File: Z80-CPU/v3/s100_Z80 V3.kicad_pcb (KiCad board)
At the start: 2 copper layers, 254 x 134.6 mm, 164 parts, among them K1 CONN_3, K10 U15 Clock, K11 bA13, K12 bA12, K13 bA19, K14 bA18, K15 bA16, K16 bA17, K17 EN_WAITS, K18 ROM_E-, K2 CONN_3, K3 pSYNCdata, K4 CONN_3, K5 pSYNC, K6 bA15, K7 bA14, K8 WRstrobe, K9 U29B Q, P1 S100_MALE, P2 CONN_4X2, P3 CLK_CPU, P34 CONN_1, P35 CONN_1, P36 CONN_3X2, P4 CONN_2X2, P5 CLK_CPU, P6 MASTER_OSC, P7 CLK_SEL, Q2 ^^NPN-SOT23, Q3 ^^NPN-SOT23, Q4 ^^NPN-SOT23, Q5 ^^NPN-SOT23, Q6 ^^NPN-SOT23, Q7 ^^NPN-SOT23, SW1 DIPS_08, SW2 DIPS_08, SW3 DIPS_08, SW4 DIPS_08, U1 Z80, U10 74LS165, U11 74LS165, U12 ^^74LS541, U13 2732, U14 74LS682N, U15 74LS165, U16 74LS273, U17 74LS273, U18 74LS161, U19 ^^74LS541, U2 ^^74LS541, U20 ^^74LS541, U21 ^^74LS541, U22 ^^74LS541, U23 74LS02, U24 74LS04, U25 74LS04, U26 ^^LOGO1, U27 74LS139, U28 74LS00, U29 74LS74, U3 ^^74LS541, U30 ^^74LS541, U31 74LS00, U32 ^^74LS541, U33 74LS74, U34 74LS74, U35 74LS32, U36 74LS04, U37 74LS05, U38 74F04, U39 74LS02, U4 74LS153, U40 74S00, U41 ^^74LS541, U45 74LS02, U48 LDO_REG_7805, U5 74LS157, U6 74LS153, U7 74LS32, U8 74LS157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

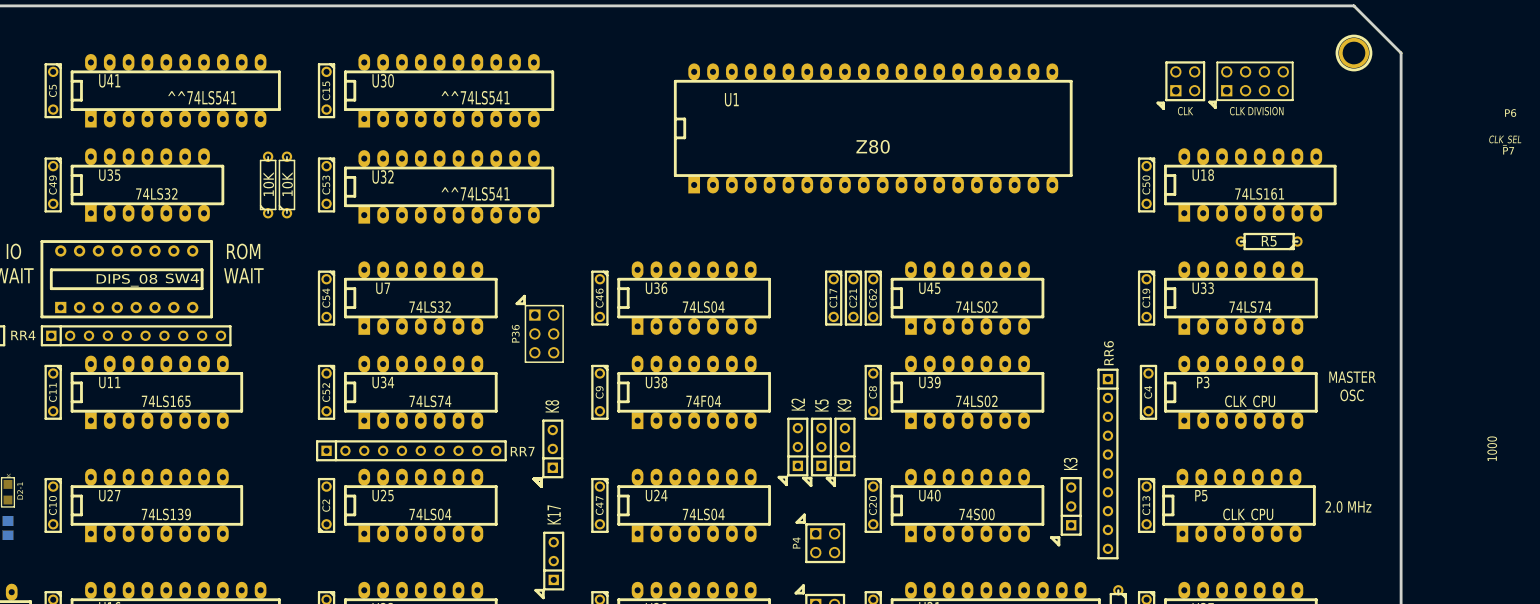
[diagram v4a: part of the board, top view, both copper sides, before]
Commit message: Z80-CPU v3: board layout (unrouted)
Source: S100 Z80 version3/backups/23-07-2014 0840
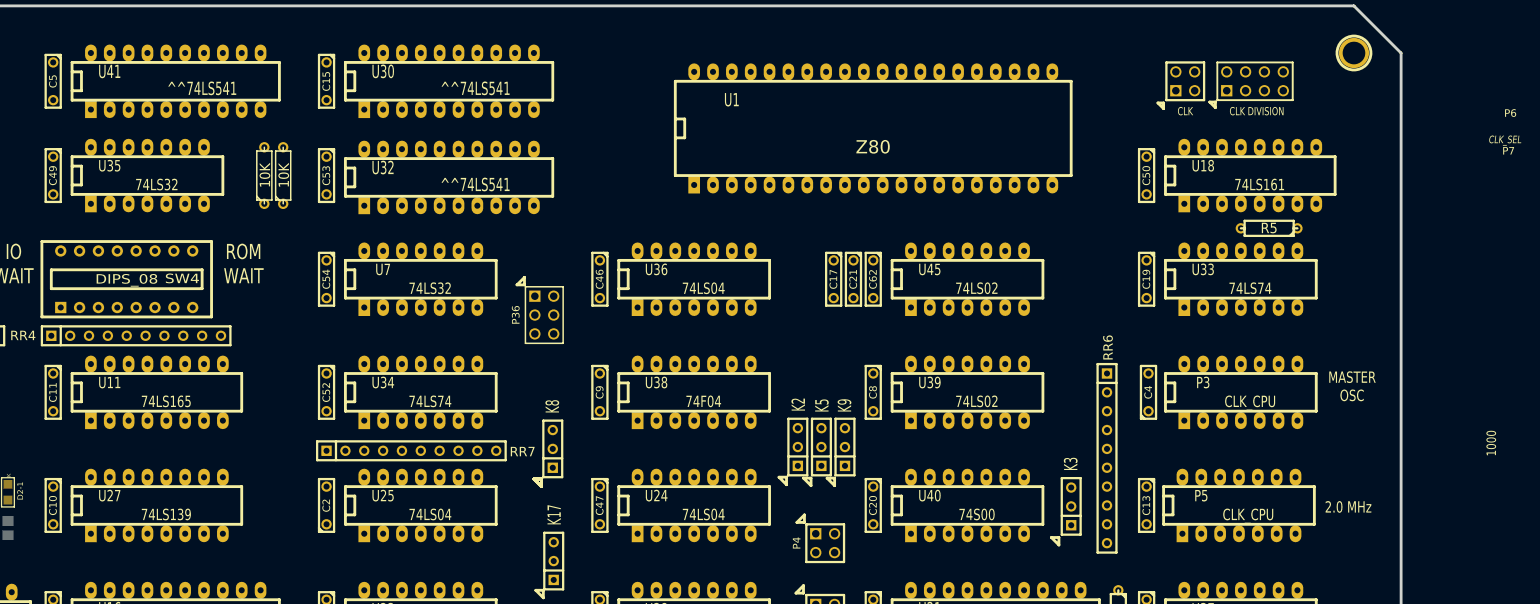
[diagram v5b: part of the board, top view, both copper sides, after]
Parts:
- moved C17 2.54 mm to (190.2, 59.7)
- moved C19 2.54 mm to (232.4, 59.7)
- moved C21 2.54 mm to (192.9, 59.7)
- moved C46 2.54 mm to (158.8, 59.7)
- moved C54 2.54 mm to (121.9, 59.7)
- moved C62 2.54 mm to (195.6, 59.7)
- moved U33 2.54 mm to (245.1, 59.7)
- moved U36 2.54 mm to (171.4, 59.7)
- moved U45 2.54 mm to (208.3, 59.7)
- moved U7 2.54 mm to (134.6, 59.7)
- moved P36 2.54 mm to (151.3, 64.5)
- moved R5 1.78 mm to (248.9, 52.8)
- moved R11 1.37 mm to (113.5, 45.7)
- moved R16 1.37 mm to (116.1, 45.7)
- moved C49 1.27 mm to (85.1, 45.7)
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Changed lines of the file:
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@@
     (area 12.509499 22.669499 266.890501 157.670501)
     (thickness 1.6002)
-    (drawings 133)
+    (drawings 137)
     (tracks 0)
     (zones 0)
@@
   )
   (module C2 (layer Top)
-    (at 121.92 34.29 270)
+    (at 121.92 33.02 270)
     (descr "Condensateur = 2 pas")
     (tags C)
@@
   )
   (module C2 (layer Top)
-    (at 232.41 62.23 270)
+    (at 232.41 59.69 270)
     (descr "Condensateur = 2 pas")
     (tags C)
@@
   )
   (module C2 (layer Top)
-    (at 158.75 62.23 270)
+    (at 158.75 59.69 270)
     (descr "Condensateur = 2 pas")
     (tags C)
@@
   )
   (module C2 (layer Top)
-    (at 85.09 46.99 270)
+    (at 85.09 45.72 270)
     (descr "Condensateur = 2 pas")
     (tags C)
@@
   )
   (module C2 (layer Top)
-    (at 121.92 62.23 270)
+    (at 121.92 59.69 270)
     (descr "Condensateur = 2 pas")
     (tags C)
@@
   )
   (module C2 (layer Top)
-    (at 232.41 46.99 270)
+    (at 232.41 45.72 270)
     (descr "Condensateur = 2 pas")
     (tags C)
@@
   )
   (module C2 (layer Top)
-    (at 121.92 46.99 270)
+    (at 121.92 45.72 270)
     (descr "Condensateur = 2 pas")
     (tags C)
@@
   )
   (module R3 (layer Top)
-    (at 248.92 54.61 180)
+    (at 248.92 52.832 180)
     (descr "Resitance 3 pas")
     (tags R)
@@
   )
   (module C2 (layer Top)
-    (at 195.58 62.23 270)
+    (at 195.58 59.69 270)
     (descr "Condensateur = 2 pas")
     (tags C)
@@
   )
   (module r_pack9 (layer Top)
-    (at 227.203 84.582 270)
+    (at 227.076 83.82 270)
     (descr "Connecteur 10 pins")
     (tags "CONN DEV")
@@
   )
   (module pin_array_3x2 (layer Top)
-    (at 151.257 67.056 270)
+    (at 151.257 64.516 270)
     (descr "Double rangee de contacts 2 x 4 pins")
     (tags CONN)
@@
   )
   (module DIP-14__300_ELL (layer Top)
-    (at 134.62 62.23)
+    (at 134.62 59.69)
     (descr "14 pins DIL package, elliptical pads")
     (tags DIL)
@@
   )
   (module DIP-14__300_ELL (layer Top)
-    (at 208.28 62.23)
+    (at 208.28 59.69)
     (descr "14 pins DIL package, elliptical pads")
     (tags DIL)
@@
   )
   (module DIP-14__300_ELL (layer Top)
-    (at 171.45 62.23)
+    (at 171.45 59.69)
     (descr "14 pins DIL package, elliptical pads")
     (tags DIL)
@@
   )
   (module DIP-14__300_ELL (layer Top)
-    (at 97.79 46.99)
+    (at 97.79 45.72)
     (descr "14 pins DIL package, elliptical pads")
     (tags DIL)
@@
   )
   (module DIP-14__300_ELL (layer Top)
-    (at 245.11 62.23)
+    (at 245.11 59.69)
     (descr "14 pins DIL package, elliptical pads")
     (tags DIL)
@@
   )
   (module DIP-16__300_ELL (layer Top)
-    (at 246.38 46.99)
+    (at 246.38 45.72)
     (descr "16 pins DIL package, elliptical pads")
     (tags DIL)
@@
   )
   (module C2 (layer Top)
-    (at 192.913 62.23 270)
+    (at 192.913 59.69 270)
     (descr "Condensateur = 2 pas")
     (tags C)
@@
   )
   (module C2 (layer Top)
-    (at 190.246 62.23 270)
+    (at 190.246 59.69 270)
     (descr "Condensateur = 2 pas")
     (tags C)
@@
   )
   (module R3 (layer Top)
-    (at 114.046 46.99 90)
+    (at 113.538 45.72 90)
     (descr "Resitance 3 pas")
     (tags R)
@@
   )
   (module R3 (layer Top)
-    (at 116.586 46.99 90)
+    (at 116.078 45.72 90)
     (descr "Resitance 3 pas")
     (tags R)
@@
   )
   (module DIP-20__300_ELL (layer Top)
-    (at 138.43 34.29)
+    (at 138.43 33.02)
     (descr "20 pins DIL package, elliptical pads")
     (tags DIL)
@@
   )
   (module DIP-20__300_ELL (layer Top)
-    (at 138.43 47.244)
+    (at 138.43 45.974)
     (descr "20 pins DIL package, elliptical pads")
     (tags DIL)
@@
   )
   (module DIP-20__300_ELL (layer Top)
-    (at 101.6 34.29)
+    (at 101.6 33.02)
     (descr "20 pins DIL package, elliptical pads")
     (tags DIL)
@@
   )
   (module C2 (layer Top)
-    (at 85.09 34.29 270)
+    (at 85.09 33.02 270)
     (descr "Condensateur = 2 pas")
     (tags C)
@@
     )
   )
+  (gr_line (start 12.192 29.21) (end 272.034 29.21) (angle 90) (layer Dwgs.User) (width 0.381))
+  (gr_line (start 13.208 41.91) (end 271.018 41.91) (angle 90) (layer Dwgs.User) (width 0.381))
+  (dimension 13.97 (width 0.3048) (layer Dwgs.User)
+    (gr_text "0.5500 in" (at 9.0424 34.925 90) (layer Dwgs.User)
+      (effects (font (size 2.032 1.524) (thickness 0.3048)))
+    )
+    (feature1 (pts (xy 12.7 27.94) (xy 7.4168 27.94)))
+    (feature2 (pts (xy 12.7 41.91) (xy 7.4168 41.91)))
+    (crossbar (pts (xy 10.668 41.91) (xy 10.668 27.94)))
+    (arrow1a (pts (xy 10.668 27.94) (xy 11.25442 29.066503)))
+    (arrow1b (pts (xy 10.668 27.94) (xy 10.08158 29.066503)))
+    (arrow2a (pts (xy 10.668 41.91) (xy 11.25442 40.783497)))
+    (arrow2b (pts (xy 10.668 41.91) (xy 10.08158 40.783497)))
+  )
+  (dimension 13.97 (width 0.3048) (layer Dwgs.User)
+    (gr_text "0.5500 in" (at 9.0424 48.895 90) (layer Dwgs.User)
+      (effects (font (size 2.032 1.524) (thickness 0.3048)))
+    )
+    (feature1 (pts (xy 12.7 41.91) (xy 7.4168 41.91)))
+    (feature2 (pts (xy 12.7 55.88) (xy 7.4168 55.88)))
+    (crossbar (pts (xy 10.668 55.88) (xy 10.668 41.91)))
+    (arrow1a (pts (xy 10.668 41.91) (xy 11.25442 43.036503)))
+    (arrow1b (pts (xy 10.668 41.91) (xy 10.08158 43.036503)))
+    (arrow2a (pts (xy 10.668 55.88) (xy 11.25442 54.753497)))
+    (arrow2b (pts (xy 10.668 55.88) (xy 10.08158 54.753497)))
+  )
+  (dimension 15.24 (width 0.3048) (layer Dwgs.User)
+    (gr_text "0.6000 in" (at 5.4864 33.02 90) (layer Dwgs.User)
+      (effects (font (size 2.032 1.524) (thickness 0.3048)))
+    )
+    (feature1 (pts (xy 12.7 25.4) (xy 3.8608 25.4)))
+    (feature2 (pts (xy 12.7 40.64) (xy 3.8608 40.64)))
+    (crossbar (pts (xy 7.112 40.64) (xy 7.112 25.4)))
+    (arrow1a (pts (xy 7.112 25.4) (xy 7.69842 26.526503)))
+    (arrow1b (pts (xy 7.112 25.4) (xy 6.52558 26.526503)))
+    (arrow2a (pts (xy 7.112 40.64) (xy 7.69842 39.513497)))
+    (arrow2b (pts (xy 7.112 40.64) (xy 6.52558 39.513497)))
+  )
+  (dimension 15.24 (width 0.3048) (layer Dwgs.User)
+    (gr_text "0.6000 in" (at 5.9944 48.26 90) (layer Dwgs.User)
+      (effects (font (size 2.032 1.524) (thickness 0.3048)))
+    )
+    (feature1 (pts (xy 12.7 40.64) (xy 4.3688 40.64)))
+    (feature2 (pts (xy 12.7 55.88) (xy 4.3688 55.88)))
+    (crossbar (pts (xy 7.62 55.88) (xy 7.62 40.64)))
+    (arrow1a (pts (xy 7.62 40.64) (xy 8.20642 41.766503)))
+    (arrow1b (pts (xy 7.62 40.64) (xy 7.03358 41.766503)))
+    (arrow2a (pts (xy 7.62 55.88) (xy 8.20642 54.753497)))
+    (arrow2b (pts (xy 7.62 55.88) (xy 7.03358 54.753497)))
+  )
   (gr_line (start 22.098 51.054) (end 23.114 51.054) (angle 90) (layer F.SilkS) (width 0.381))
   (gr_line (start 23.114 52.07) (end 22.098 51.054) (angle 90) (layer F.SilkS) (width 0.381))
@@
   (gr_line (start 84.836 141.478) (end 83.82 142.494) (angle 90) (layer F.SilkS) (width 0.381))
   (gr_line (start 84.836 142.494) (end 84.836 141.478) (angle 90) (layer F.SilkS) (width 0.381))
-  (gr_line (start 147.574 62.992) (end 148.59 62.992) (angle 90) (layer F.SilkS) (width 0.381))
-  (gr_line (start 148.59 61.976) (end 147.574 62.992) (angle 90) (layer F.SilkS) (width 0.381))
-  (gr_line (start 148.59 62.992) (end 148.59 61.976) (angle 90) (layer F.SilkS) (width 0.381))
+  (gr_line (start 147.574 60.452) (end 148.59 60.452) (angle 90) (layer F.SilkS) (width 0.381))
+  (gr_line (start 148.59 59.436) (end 147.574 60.452) (angle 90) (layer F.SilkS) (width 0.381))
+  (gr_line (start 148.59 60.452) (end 148.59 59.436) (angle 90) (layer F.SilkS) (width 0.381))
   (gr_line (start 150.876 87.63) (end 150.876 86.614) (angle 90) (layer F.SilkS) (width 0.381))
   (gr_line (start 149.86 86.614) (end 150.876 87.63) (angle 90) (layer F.SilkS) (width 0.381))
@@
   )
   (gr_line (start 232.41 139.954) (end 232.41 10.668) (angle 90) (layer Dwgs.User) (width 0.381))
-  (gr_line (start 11.684 30.48) (end 270.51 30.48) (angle 90) (layer Dwgs.User) (width 0.381))
   (dimension 12.7 (width 0.3048) (layer Dwgs.User)
     (gr_text "0.5000 in" (at 2.4384 36.83 90) (layer Dwgs.User)
@@
     (arrow2b (pts (xy 4.064 43.18) (xy 3.47758 42.053497)))
   )
-  (gr_line (start 12.7 43.18) (end 273.558 43.18) (angle 90) (layer Dwgs.User) (width 0.381))
   (dimension 12.7 (width 0.3048) (layer Dwgs.User)
     (gr_text "0.5000 in" (at 2.4384 49.53 90) (layer Dwgs.User)

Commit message: Z80-CPU v3: schematic trimmed, re-placement
Source: S100 Z80 version3/backups/24-07-2014 end of day
Newest file is 2014-07-23 14:45; the folder name says 24-07.
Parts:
- removed C16, C24, C29, C5, C53, C58: 0.1 uF, C2
- removed C6: 0.022 uF, C1V7
- removed D3, D4, D5, D7: DONE, ^^LED-0805
- removed D9: D2-1, ^^LED-0805
- removed Q4, Q5, Q6, Q7: ^^NPN-SOT23, ^^-SOT23
- removed R10, R13, R15, R8: 470, ^^SMD_Resistor-0805
- removed R12, R14, R42, R9: 330, ^^SMD_Resistor-0805
- removed U16, U17: 74LS273, DIP-20__300_ELL
- removed U23: 74LS02, DIP-14__300_ELL
- removed U4, U6: 74LS153, DIP-16__300_ELL
- removed U5: 74LS157, DIP-16__300_ELL
- added P8: CONN_20, ^^SIL-20, F.Cu at (50.5, 52.5)
- added P9: CONN_20, ^^SIL-20, F.Cu at (50.5, 97.5)
- Q2, Q3: value ^^NPN-SOT23 -> NPN; footprint ^^-SOT23 -> ^^TO92-inline; moved to F.Cu
- R1, R2, R3, R6: footprint ^^SMD_Resistor-0805 -> R3; moved to F.Cu
- R7: value 330 -> 1K; footprint ^^SMD_Resistor-0805 -> R3; moved to F.Cu
- moved U29 137.2 mm to (171.4, 120.8)
- moved K4 117.7 mm to (147.2, 59.7)
- moved R7 113.9 mm to (150.4, 59.7), turned to 90 degrees
- moved K18 94.3 mm to (118.1, 59.7)
- moved U31 72.0 mm to (134.6, 105.7)
- moved K10 65.7 mm to (80.5, 120.7)
- moved C10 65.1 mm to (21.8, 74.9)
- moved U11 63.5 mm to (35.6, 75.1)
- moved RR4 59.6 mm to (36.7, 68.1)
- moved U41 53.5 mm to (68.5, 75.1)
- moved U27 47.9 mm to (135.9, 120.8)
- moved SW4 47.2 mm to (93.2, 106.8)
- moved U32 47.1 mm to (101.3, 75.1)
- moved SW3 47.0 mm to (63.2, 106.7)
- moved SW2 47.0 mm to (33.3, 106.7)
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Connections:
- K11 pad 3: N-0000087 (its old number) -> /U4p9
- K12 pad 3: N-0000088 (its old number) -> /U4p7
- K13 pad 3: N-0000071 (its old number) -> /U5p4
- K14 pad 3: N-0000072 -> /U5p7
- K15 pad 3: N-0000073 -> /U5p12
- K16 pad 3: N-0000074 -> /U5p9
- K4 pad 3: /RR4p10 -> N-00000114
- K6 pad 3: N-0000083 (its old number) -> /U6p9
- K7 pad 3: N-0000085 (its old number) -> /U6p7
- Q2 pad 1: N-0000011 (its old number) -> GND
- Q2 pad 2: GND -> N-0000010
- Q3 pad 1: N-0000014 (its old number) -> GND
- Q3 pad 2: GND -> N-0000013
- R2 pad 1: N-0000011 (its old number) -> N-0000010
- R6 pad 1: N-0000014 (its old number) -> N-0000013
- R7 pad 1: N-000003 -> VCC
- R7 pad 2: VCC -> N-00000114
- RR2 pad 10: /RR4p10 -> (no net)
- U1 pad 26: /RESET* -> /PU5K-C
- U25 pad 5: /bA14 -> (no net)
- U25 pad 6: N-0000028 (its old number) -> (no net)
- U34 pad 10: /RESET* -> /PU5K-C
- U8 pad 1: /IORQ -> /IORQ+
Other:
- board text removed: "A16"
- board text removed: "A17"
- board text removed: "A18"
- board text removed: "A19"

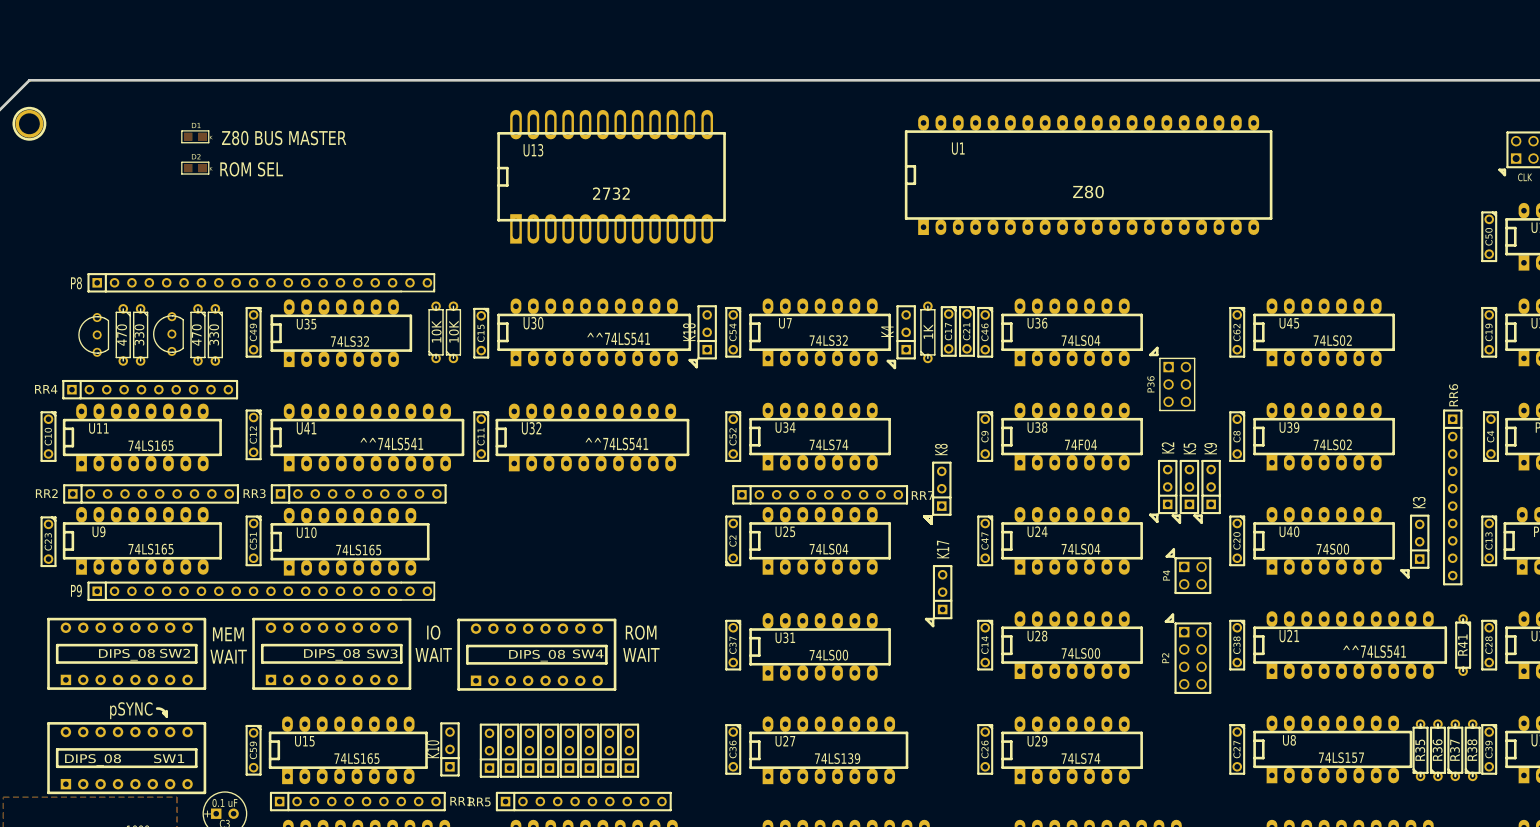
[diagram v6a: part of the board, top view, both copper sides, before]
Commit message: Z80-CPU v3: schematic and placement
Source: S100 Z80 version3/backups/27-07-2014 1407
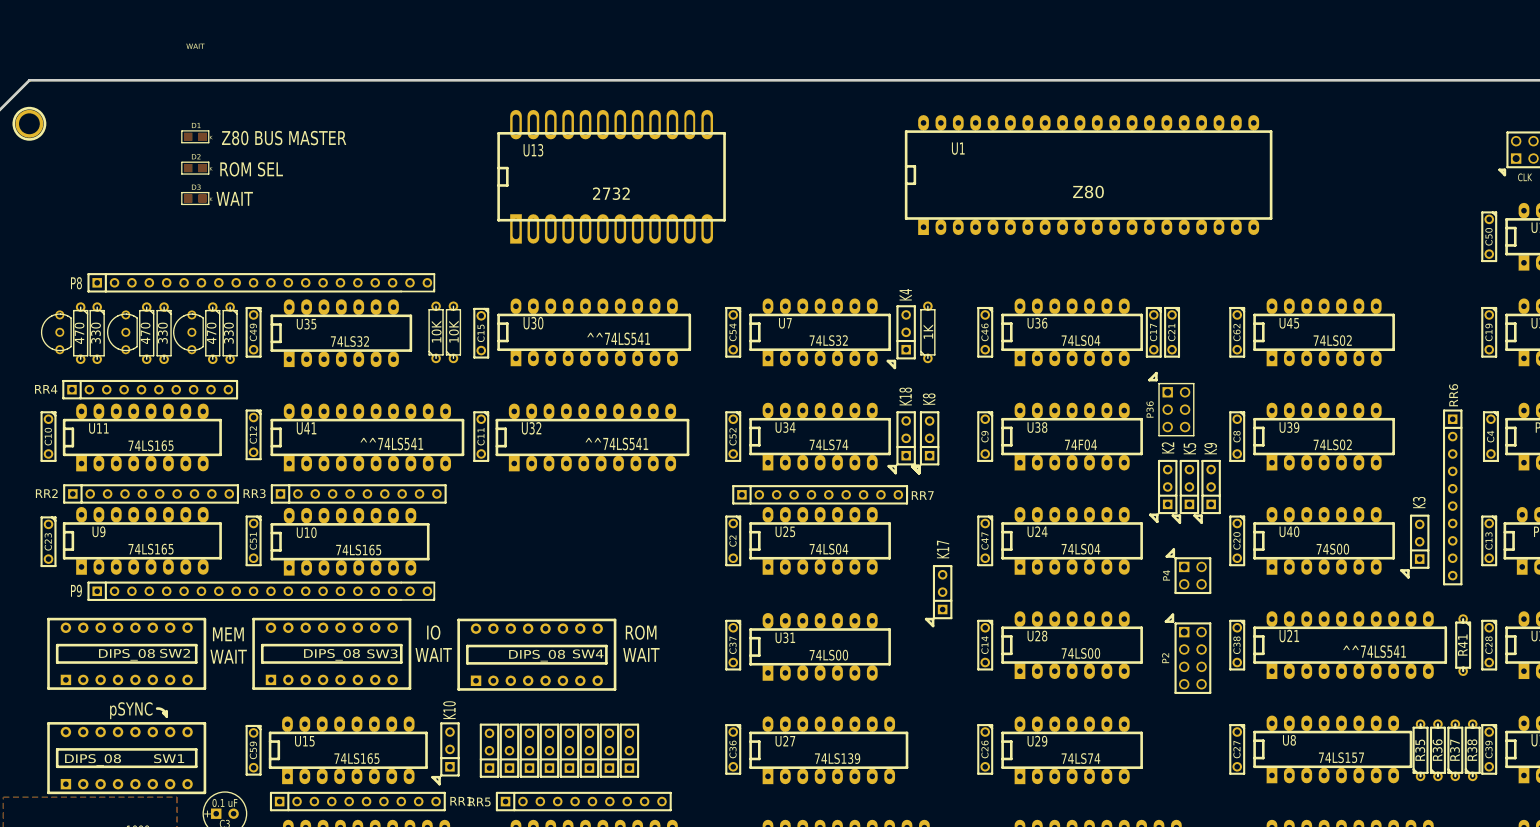
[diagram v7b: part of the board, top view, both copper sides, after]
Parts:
- added D3: WAIT, ^^LED-0805, F.Cu at (43.3, 40.1)
- added Q1: NPN, ^^TO92-inline, F.Cu at (23.5, 59.7)
- added R8: 330, R3, F.Cu at (29.0, 59.8)
- added R9: 470, R3, F.Cu at (26.5, 59.8)
- moved K18 33.0 mm to (147.2, 75.2)
- moved C17 30.0 mm to (183.4, 59.7)
- moved C21 30.0 mm to (186.1, 59.7)
- moved K8 7.58 mm to (150.6, 75.2)
- moved Q3 4.21 mm to (33.1, 59.7)
- moved P36 3.69 mm to (186.7, 71.0)
- moved R3 3.44 mm to (38.7, 59.8)
- moved R6 3.44 mm to (36.2, 59.8)
- moved Q2 2.93 mm to (42.8, 59.7)
- moved R1 2.17 mm to (48.4, 59.8)
- moved R2 2.17 mm to (45.8, 59.8)
- turned C2 to 270 degrees
- turned C4 to 270 degrees
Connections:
- K1 pad 3: /NMI* -> /NMI*s100
- P1 pad 12: /NMI* -> /NMI*s100
- P8 pad 18: (no net) -> /bA2
- P8 pad 19: (no net) -> /bA3
- P8 pad 20: (no net) -> /bA5
- P9 pad 10: (no net) -> /IORQ*
- P9 pad 11: (no net) -> /WR*
- P9 pad 12: (no net) -> /RD*
- P9 pad 13: (no net) -> /bA0
- P9 pad 14: (no net) -> /bA1
- P9 pad 15: (no net) -> /bA6
- P9 pad 16: (no net) -> /bA7
- P9 pad 17: GND -> /ROM_E-33
- P9 pad 9: (no net) -> /MREQ*
- U22 pad 6: /WR* -> /sWO*b
- U25 pad 13: N-0000082 (its old number) -> /WAIT+
- U31 pad 3: N-0000082 (its old number) -> /WAIT+
- U35 pad 11: (no net) -> /sWO*b
- U35 pad 12: (no net) -> N-00000123
- U35 pad 13: (no net) -> /WR*
- U41 pad 14: (no net) -> /ROM_E-
- U41 pad 6: (no net) -> /ROM_E-33
- U45 pad 4: (no net) -> N-00000123
- U45 pad 5: (no net) -> /REFSH*
- U45 pad 6: (no net) -> /REFSH*
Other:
- board text added: "WAIT"
